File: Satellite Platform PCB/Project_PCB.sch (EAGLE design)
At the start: 32 parts, among them IC1 A4990KLPTR-T, IC4 A4990KLPTR-T

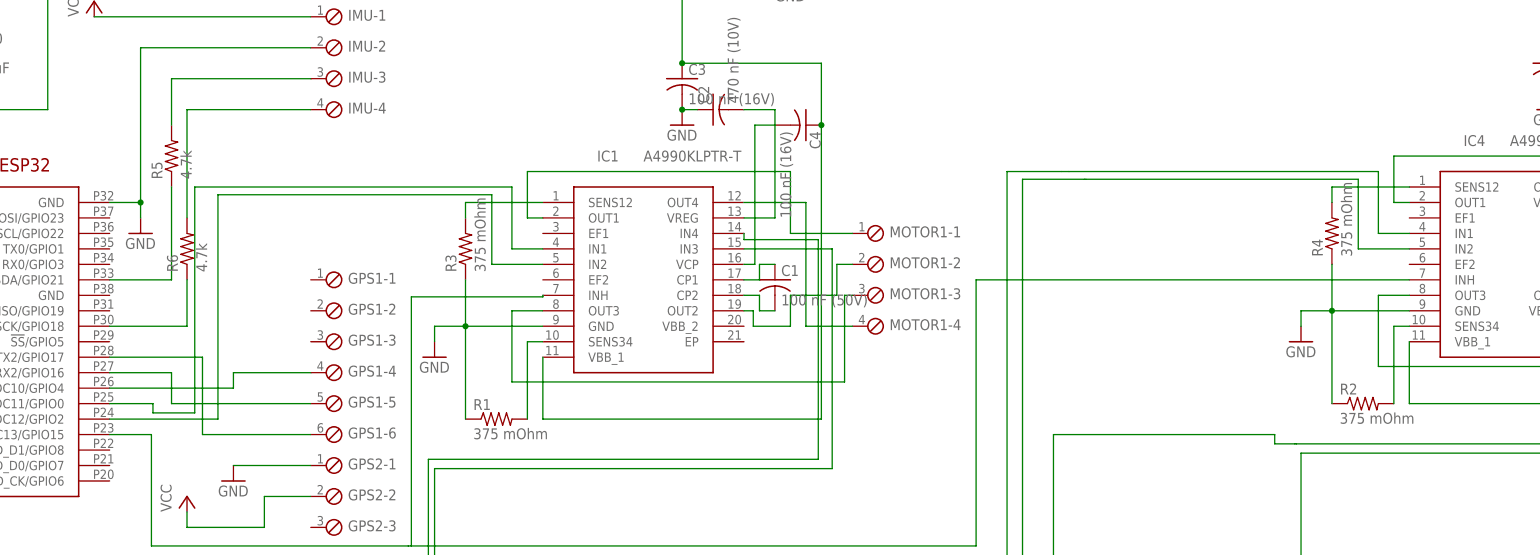
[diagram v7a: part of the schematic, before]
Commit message: Added Pin Labels
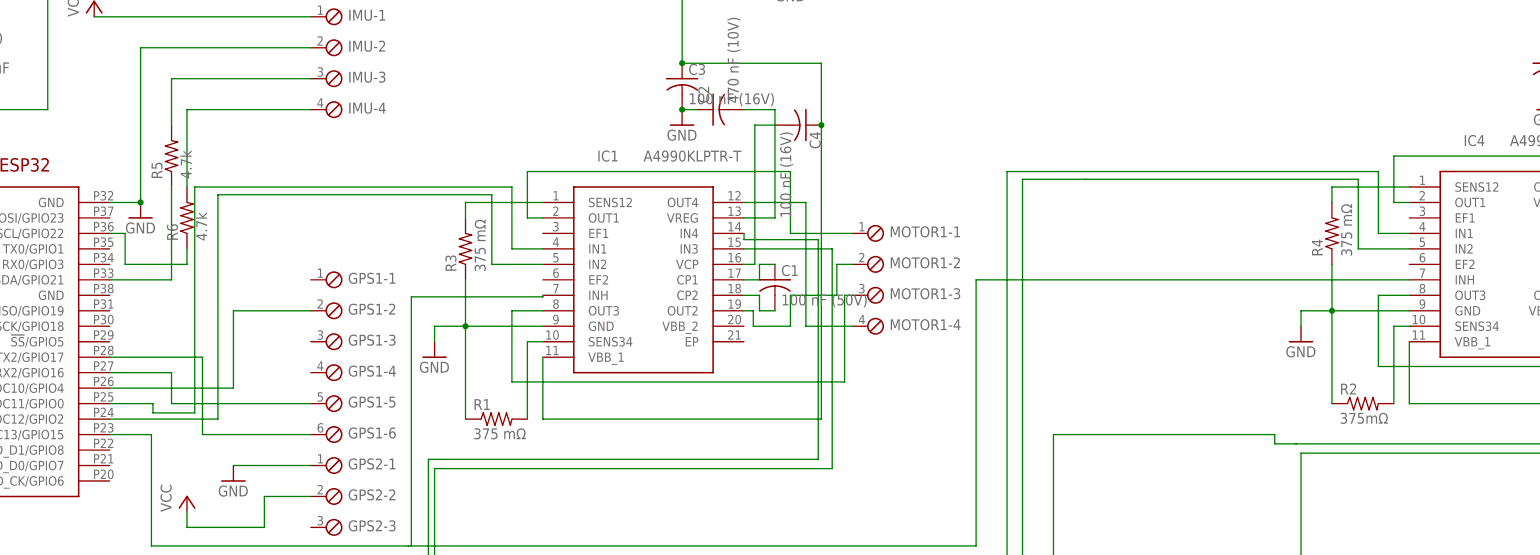
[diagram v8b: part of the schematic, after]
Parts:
- R1, R3, R4: value 375 mOhm -> 375 mΩ
- R2: value 375 mOhm -> 375mΩ
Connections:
- removed net N$44: R6.1, U$1.SCK/GPIO18
- new net N$36: R6.1, U$1.SCL/GPIO22
- net N$5: now also GPS1-2.1; no longer GPS1-4.1
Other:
- moved on the sheet: R6
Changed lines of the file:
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@@
 <part name="C3" library="rcl" library_urn="urn:adsk.eagle:library:334" deviceset="C-US" device="C0805" package3d_urn="urn:adsk.eagle:package:23617/2" value="100 nF (16V)"/>
 <part name="C4" library="rcl" library_urn="urn:adsk.eagle:library:334" deviceset="C-US" device="C0805" package3d_urn="urn:adsk.eagle:package:23617/2" value="100 nF (16V)"/>
-<part name="R1" library="rcl" library_urn="urn:adsk.eagle:library:334" deviceset="R-US_" device="R0805" package3d_urn="urn:adsk.eagle:package:23553/2" value="375 mOhm"/>
-<part name="R3" library="rcl" library_urn="urn:adsk.eagle:library:334" deviceset="R-US_" device="R0805" package3d_urn="urn:adsk.eagle:package:23553/2" value="375 mOhm"/>
+<part name="R1" library="rcl" library_urn="urn:adsk.eagle:library:334" deviceset="R-US_" device="R0805" package3d_urn="urn:adsk.eagle:package:23553/2" value="375 mΩ"/>
+<part name="R3" library="rcl" library_urn="urn:adsk.eagle:library:334" deviceset="R-US_" device="R0805" package3d_urn="urn:adsk.eagle:package:23553/2" value="375 mΩ"/>
 <part name="GND1" library="supply1" library_urn="urn:adsk.eagle:library:371" deviceset="GND" device=""/>
 <part name="GND8" library="supply1" library_urn="urn:adsk.eagle:library:371" deviceset="GND" device=""/>
@@
 <part name="C7" library="rcl" library_urn="urn:adsk.eagle:library:334" deviceset="C-US" device="C0805" package3d_urn="urn:adsk.eagle:package:23617/2" value="100 nF (16V)"/>
 <part name="C8" library="rcl" library_urn="urn:adsk.eagle:library:334" deviceset="C-US" device="C0805" package3d_urn="urn:adsk.eagle:package:23617/2" value="100 nF (16V)"/>
-<part name="R2" library="rcl" library_urn="urn:adsk.eagle:library:334" deviceset="R-US_" device="R0805" package3d_urn="urn:adsk.eagle:package:23553/2" value="375 mOhm"/>
-<part name="R4" library="rcl" library_urn="urn:adsk.eagle:library:334" deviceset="R-US_" device="R0805" package3d_urn="urn:adsk.eagle:package:23553/2" value="375 mOhm"/>
+<part name="R2" library="rcl" library_urn="urn:adsk.eagle:library:334" deviceset="R-US_" device="R0805" package3d_urn="urn:adsk.eagle:package:23553/2" value="375mΩ"/>
+<part name="R4" library="rcl" library_urn="urn:adsk.eagle:library:334" deviceset="R-US_" device="R0805" package3d_urn="urn:adsk.eagle:package:23553/2" value="375 mΩ"/>
 <part name="GND9" library="supply1" library_urn="urn:adsk.eagle:library:371" deviceset="GND" device=""/>
 <part name="GND10" library="supply1" library_urn="urn:adsk.eagle:library:371" deviceset="GND" device=""/>
@@
 <attribute name="VALUE" x="111.76" y="109.22" size="1.778" layer="96"/>
 </instance>
-<instance part="GND6" gate="1" x="7.62" y="71.12" smashed="yes">
-<attribute name="VALUE" x="5.08" y="68.58" size="1.778" layer="96"/>
+<instance part="GND6" gate="1" x="7.62" y="73.66" smashed="yes">
+<attribute name="VALUE" x="5.08" y="71.12" size="1.778" layer="96"/>
 </instance>
 <instance part="P+1" gate="VCC" x="-48.26" y="88.9" smashed="yes">
@@
 <attribute name="VALUE" x="16.002" y="80.01" size="1.778" layer="96" rot="R90"/>
 </instance>
-<instance part="R6" gate="G$1" x="15.24" y="68.58" smashed="yes" rot="R90">
-<attribute name="NAME" x="13.7414" y="64.77" size="1.778" layer="95" rot="R90"/>
-<attribute name="VALUE" x="18.542" y="64.77" size="1.778" layer="96" rot="R90"/>
+<instance part="R6" gate="G$1" x="15.24" y="73.66" smashed="yes" rot="R90">
+<attribute name="NAME" x="13.7414" y="69.85" size="1.778" layer="95" rot="R90"/>
+<attribute name="VALUE" x="18.542" y="69.85" size="1.778" layer="96" rot="R90"/>
 </instance>
 <instance part="LT1129" gate="G$1" x="-33.02" y="111.76" smashed="yes">
@@
 <pinref part="U$1" gate="G$1" pin="GND@1"/>
 <wire x1="2.54" y1="76.2" x2="7.62" y2="76.2" width="0.1524" layer="91"/>
-<wire x1="7.62" y1="76.2" x2="7.62" y2="73.66" width="0.1524" layer="91"/>
 <pinref part="GND6" gate="1" pin="GND"/>
 <pinref part="IMU" gate="-2" pin="1"/>
@@
 <pinref part="U$1" gate="G$1" pin="ADC10/GPIO4"/>
 <wire x1="2.54" y1="45.72" x2="22.86" y2="45.72" width="0.1524" layer="91"/>
-<wire x1="22.86" y1="45.72" x2="22.86" y2="48.26" width="0.1524" layer="91"/>
-<pinref part="GPS1" gate="-4" pin="1"/>
-<wire x1="22.86" y1="48.26" x2="35.56" y2="48.26" width="0.1524" layer="91"/>
+<pinref part="GPS1" gate="-2" pin="1"/>
+<wire x1="35.56" y1="58.42" x2="22.86" y2="58.42" width="0.1524" layer="91"/>
+<wire x1="22.86" y1="58.42" x2="22.86" y2="45.72" width="0.1524" layer="91"/>
 </segment>
 </net>
@@
 <wire x1="35.56" y1="91.44" x2="15.24" y2="91.44" width="0.1524" layer="91"/>
 <pinref part="R6" gate="G$1" pin="2"/>
-<wire x1="15.24" y1="91.44" x2="15.24" y2="73.66" width="0.1524" layer="91"/>
+<wire x1="15.24" y1="91.44" x2="15.24" y2="78.74" width="0.1524" layer="91"/>
 </segment>
 </net>
@@
 </segment>
 </net>
-<net name="N$44" class="0">
-<segment>
-<pinref part="U$1" gate="G$1" pin="SCK/GPIO18"/>
-<wire x1="15.24" y1="55.88" x2="2.54" y2="55.88" width="0.1524" layer="91"/>
-<pinref part="R6" gate="G$1" pin="1"/>
-<wire x1="15.24" y1="63.5" x2="15.24" y2="55.88" width="0.1524" layer="91"/>
-</segment>
-</net>
 <net name="N$46" class="0">
 <segment>
@@
 </segment>
 </net>
+<net name="N$36" class="0">
+<segment>
+<pinref part="R6" gate="G$1" pin="1"/>
+<wire x1="15.24" y1="68.58" x2="15.24" y2="66.04" width="0.1524" layer="91"/>
+<wire x1="15.24" y1="66.04" x2="5.08" y2="66.04" width="0.1524" layer="91"/>
+<pinref part="U$1" gate="G$1" pin="SCL/GPIO22"/>
+<wire x1="5.08" y1="66.04" x2="5.08" y2="71.12" width="0.1524" layer="91"/>
+<wire x1="5.08" y1="71.12" x2="2.54" y2="71.12" width="0.1524" layer="91"/>
+</segment>
+</net>
